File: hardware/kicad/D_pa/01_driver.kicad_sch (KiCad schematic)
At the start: 27 parts, among them J10 A kartindan TX1, Q20 IRF530N, Q21 IRF530N, T10 BN43-202 2:1, T12 BN43-202 2:3 CT, U10 PE4312C-Z, U11 PGA-103+

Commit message: Replace the transmit filters: harmonic suppression was illegal
Simulation of the output filters shows second-harmonic suppression
between 3 and 30 dB, where 43 dB is necessary below 30 MHz and 60 dB
above. On the 80/60 m position the second harmonic of 3.5 MHz is
3.4 dB down: the filter barely touches it. The transmitter would have
been out of specification on every band, and the board gives no sign
of it. Output power, SWR and efficiency all read correctly while the
harmonic radiates.

The cause is the band grouping. One position must pass 5.37 MHz, so
its cutoff is at 6.0, and the second harmonic of the same position's
lowest band, 3.5 MHz, falls at 7.0. More poles do not help: by the
Chebyshev attenuation formula, nine poles give 32 dB there.

Each series inductor now has a parallel capacitor that places a
transmission zero on the harmonic. 80 m and 60 m are separate
positions, because a trap at 7.0 MHz also attenuates a 5.37 MHz
passband. That uses the seventh relay, which was a bypass; a
transmitter with no harmonic filter in line is not legal in any case.

  band      loss   2nd harmonic   was
  160m      0.61   -82.4          -25.2
  80m       0.64   -80.7          grouped
  60m       0.45   -81.9          grouped
  40_30m    1.45   -58.0          -9.5
  20_17m    0.88   -68.4          -18.2
  15_10m    1.35   -61.0          -14.1
  6m        1.14   -82.8          -30.2
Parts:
- removed C110: 10uF, Capacitor_SMD:C_1206_3216Metric, symbol Device:C
- removed C110: 100nF, Capacitor_SMD:C_0603_1608Metric, symbol Device:C
- added C110: 100nF, Capacitor_SMD:C_0603_1608Metric, symbol Device:C
- added C110: 10uF, Capacitor_SMD:C_1206_3216Metric, symbol Device:C
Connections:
- net +3V3: now also C110.1
- net D2_CT: now also C110.1
- net GND: now also C110.2, C110.2

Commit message: Update the ARDC package and record the simulation results
The package had drifted from the boards again: board C's BOM was 45
lines out of date and D's 46, and the schematic PDFs predated both
filter redesigns.

The verification document gains a section on circuit simulation. Every
check before it asks which pin joins which net; none of them can say
whether a capacitor's value is correct. That section holds the
measurements for both redesigns and, separately, the three faults the
simulation tools had themselves: a source divider that made every
insertion loss 6 dB too pessimistic, an E12 rounding helper that
multiplied instead of dividing, and an inductor loss computed at a
fixed 1 MHz.

Two entries in the status were wrong. Gateware timing is closed, with
all five clocks above target rather than two below. Decoupling
placement is corrected. In their place: the remaining overlaps at the
time of writing, five points that still need datasheet confirmation,
and the stock status of the new filter values, which could not be
queried and should be checked before ordering.
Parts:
- removed C110: 100nF, Capacitor_SMD:C_0603_1608Metric, symbol Device:C
- removed C110: 10uF, Capacitor_SMD:C_1206_3216Metric, symbol Device:C
- added C110: 100nF, Capacitor_SMD:C_0603_1608Metric, symbol Device:C
- added C110: 10uF, Capacitor_SMD:C_1206_3216Metric, symbol Device:C
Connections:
- net +3V3: now also C110.1
- net D2_CT: now also C110.1
- net GND: now also C110.2, C110.2

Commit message: Name the copyright holder and stamp it into the generated files
The repository had three licence files and no statement of who owns
the work. The only record of authorship was the git author field.

Copyleft depends on that statement. GPL and CERN-OHL-S work because
the holder grants permission on condition of reciprocity; with no
holder named there is nobody to require it from a downstream user.
Naming the author keeps the design open rather than closing it.

kicad/telif.py is the single source. The line reaches the schematics
through their title block and not through the generators, because
every schematic file is rewritten on each build and a header placed in
a generator would disappear at the first regeneration. All 23
schematics carry it. 109 source files have SPDX headers, split by the
project's own table: generators and the layout chain are hardware
under CERN-OHL-S-2.0, HDL and the audit tools are software under
GPL-3.0-only.

Board C's inductors also move to footprints that match parts that can
be bought. All of them sat on 0805 pads. Of the values this design
needs, 33 to 220 nH are 0603 parts, 470 and 820 nH are 0805, and
everything from 1000 nH upward is 1210, which is 3.2 by 2.5 mm and
does not fit an 0805 land. 32 inductors could not have been soldered.

A symbol-against-footprint check cannot find this. Those two agreed
with each other; what was wrong was the body size of the real part
behind the footprint.
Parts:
- removed C110: 100nF, Capacitor_SMD:C_0603_1608Metric, symbol Device:C
- removed C110: 10uF, Capacitor_SMD:C_1206_3216Metric, symbol Device:C
- added C110: 10uF, Capacitor_SMD:C_1206_3216Metric, symbol Device:C
- added C110: 100nF, Capacitor_SMD:C_0603_1608Metric, symbol Device:C
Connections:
- net +3V3: now also C110.1
- net D2_CT: now also C110.1
- net GND: now also C110.2, C110.2

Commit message: Correct the voltage rating of the RF capacitors on board D
The BOM had no verified order code for 245 parts. The BOM program
recognised the format of a value and wrote "BASE" for all of them. It
did not examine availability.

A new tool queries the supplier. It does not accept "the part
exists". The package and the value must agree exactly. The stock must
be more than the quantity. It also reads the properties of the part.

Two faults came out of this:

The trap capacitors were 50 V parts. The carrier peak voltage is
100 V at 100 W into 50 ohms, and the voltage across the trap inductor
is 93 V. A 50 V part shows the same value in the catalogue and then
breaks down. The fault appears only when the transmitter operates.

The 1.1 pF, 1.6 pF and 3.6 pF values had no stock in the 1206
package. The same values are available in 0603 at 250 V. The smaller
package is acceptable here. This capacitor is the small half of a
pair and carries a small part of the current.

The value selection now depends on availability. The program found
the nearest pair mathematically, and one value was 3.6 pF. That value
has no stock at 250 V in any package. The small half now comes from a
list of parts that are really in stock.

The harmonic suppression did not change: 58.7 dB to 83.8 dB, against
a limit of 43 dB and 60 dB.

The filter capacitors were X7R parts. The capacitance of X7R changes
with voltage and with temperature. Every capacitor below 10 nF is now
a filter part and must be C0G or NP0.

Through-hole parts do not go into machine assembly. A separate file
lists them with the necessary specification. The BOM gave only the
value and a general footprint, and that invites the wrong purchase.
At 100 W, 1.3 A flows through the shunt capacitor at 14 MHz. A cheap
disc ceramic heats, its capacitance moves, and the filter changes.
Only full transmitter power shows this.
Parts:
- removed C110: 10uF, Capacitor_SMD:C_1206_3216Metric, symbol Device:C
- removed C110: 100nF, Capacitor_SMD:C_0603_1608Metric, symbol Device:C
- added C110: 100nF, Capacitor_SMD:C_0603_1608Metric, symbol Device:C
- added C110: 10uF, Capacitor_SMD:C_1206_3216Metric, symbol Device:C
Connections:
- net +3V3: now also C110.1
- net D2_CT: now also C110.1
- net GND: now also C110.2, C110.2

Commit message: Correct the transmit envelope and add a third zero on 15 m to 10 m
The unit has no reconstruction filter. A comment on board A said that
the filter is on board C. Board C has no such filter: the transmit
signal enters through an SMA connector and goes to the transmit and
receive relay. The datasheet also gave a cutoff frequency for this
filter that does not exist.

A sampling DAC does not make one frequency. It makes images at
|k*fs +/- fd|. The zero-order hold gives each image a different
level, and the function falls slowly. If the carrier is near Nyquist,
an image at a lower frequency can be stronger than the carrier.

A new tool measures this. It uses the harmonic filter of board D,
because that filter is the only one in the transmit path.

  15 m to 10 m   4-channel   image at 10.3 MHz is 10.4 dB stronger
  6 m            4-channel   image is 14.2 dB stronger
  6 m            2-channel   image is 7.4 dB stronger
  20 m, 17 m     4-channel   -12.0 dBc, the limit is -43 dBc
  15 m to 10 m   2-channel   -40.4 dBc, the limit is -43 dBc

Only the last one is correctable.

That filter position must attenuate three frequencies: 42 MHz (the
second harmonic of 21 MHz), 63 MHz (the third harmonic) and 50.3 MHz
(the DAC image). A five-pole filter has two traps. No pair of trap
frequencies gives more than 1.9 dB of margin, and 1.9 dB is not a
margin: one E24 rounding already cost 19 dB in this project.

A shunt series-LC at the output adds a third zero. The image goes
from -40.4 dBc to -47.3 dBc, and the margin becomes 23 dB. Above
resonance the branch is capacitive and attenuates the whole stopband,
so the harmonics also improve. The passband loss falls from 1.35 dB
to 0.99 dB.

The transmit envelope is now written honestly. The RTL said "Nyquist
is 20 MHz, so 160 m to 17 m". Nyquist alone is not enough: the images
must also be filtered, and the real limit is lower.

  4-channel   160 m to 30 m
  2-channel   160 m to 10 m
  6 m         no transmit. Receive works, with 68 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
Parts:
- removed C110: 100nF, Capacitor_SMD:C_0603_1608Metric, symbol Device:C
- removed C110: 10uF, Capacitor_SMD:C_1206_3216Metric, symbol Device:C
- added C110: 100nF, Capacitor_SMD:C_0603_1608Metric, symbol Device:C
- added C110: 10uF, Capacitor_SMD:C_1206_3216Metric, symbol Device:C
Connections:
- net +3V3: now also C110.1
- net D2_CT: now also C110.1
- net GND: now also C110.2, C110.2

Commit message: Add BIAS_KILL to remove a single-fault destruction path
Each final device has its own closed-loop bias servo: a 0.01 ohm
sense resistor, an INA240A1 with a gain of 20, an LM358 integrator,
and the gate. Separate servos are correct for paralleled MOSFETs,
because different threshold voltages make one device take most of the
current.

A new tool measures the loop in ngspice. It does not model the inside
of the MOSFET. The boundary conditions are sufficient: input
capacitance, transconductance and threshold voltage.

The loop is stable. The crossover is at 25.7 Hz, the phase margin is
90 degrees, and the current reaches the set value in 106 ms.

The failure behaviour is destructive. The integrator raises the gate
until the measured current equals the set value. If the measurement
arm opens, the measured current reads zero. The error never closes.

  the gate reaches 10.4 V in 285 ms
  57.6 A and 2878 W in each device
  the continuous limit of the IRFP250N is 214 W

All four devices fail. The protection circuit kills what it protects.

A zener clamp does not solve this. The transconductance is 8 S, so
1 V above the threshold already gives 8 A. A safe clamp voltage would
be too near the operating point.

The board sees the condition already. Board 06 says: if the quiescent
current differs from the set value by 20 percent, the bias servo is
faulty, so cut. But PA_INHIBIT removes only the driver supply. In a
class-A stage the quiescent current does the damage, not the drive.

BIAS_KILL short-circuits the integrator capacitor. A pull-down on the
gate alone is not sufficient: the integrator would stay charged at
the rail, and the gate would jump to 10.5 V when the fault clears.
With the capacitor short-circuited, the op-amp follows the set
voltage and the gate stays at 0.33 V. The threshold is 3.2 V.

The circuit is one 2N7002 that inverts PA_INHIBIT, a 10k pull-up, and
one 2N7002 across each integrator capacitor. The unpowered state is
safe: the 10k pull-downs hold the gate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
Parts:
- removed C110: 100nF, Capacitor_SMD:C_0603_1608Metric, symbol Device:C
- removed C110: 10uF, Capacitor_SMD:C_1206_3216Metric, symbol Device:C
- added C110: 10uF, Capacitor_SMD:C_1206_3216Metric, symbol Device:C
- added C110: 100nF, Capacitor_SMD:C_0603_1608Metric, symbol Device:C
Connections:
- net +3V3: now also C110.1
- net D2_CT: now also C110.1
- net GND: now also C110.2, C110.2

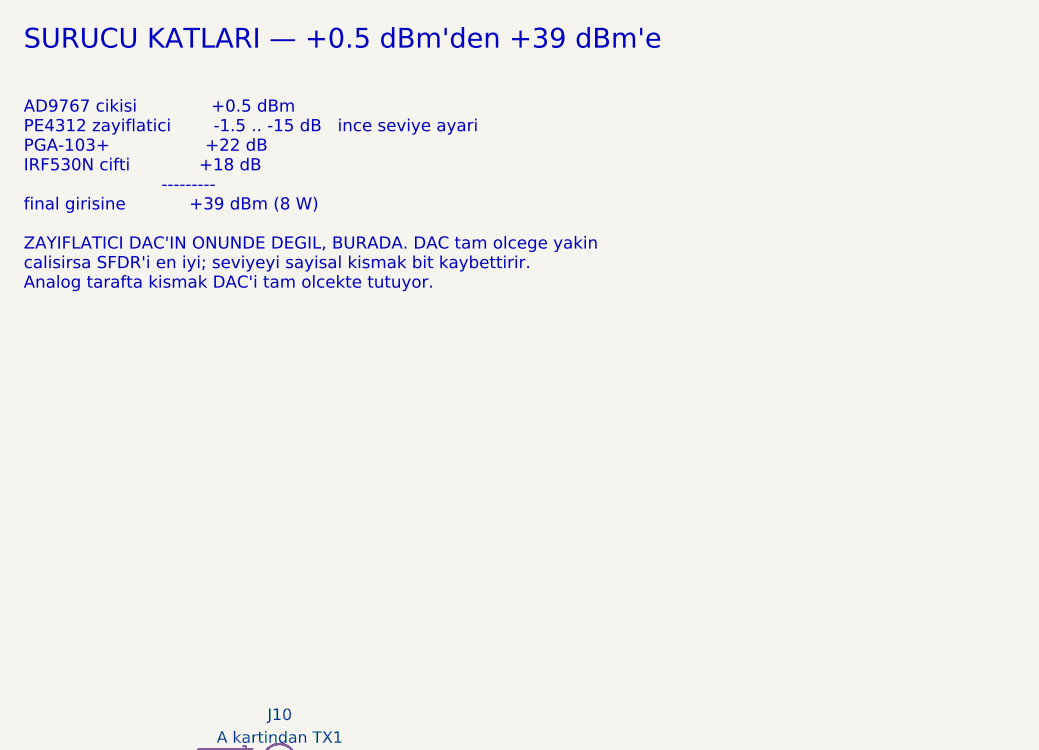
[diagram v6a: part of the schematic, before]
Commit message: Give the drive level that the final stage really needs
The budget on the schematic added the driver stages. It did not say
how much drive the final stage needs. Without that number, nobody can
tell whether the budget closes.

A new tool calculates both sides from the devices.

The output side is healthy. The quiescent current is 6.68 A, and in
class A the peak current cannot go above it. 100 W needs a peak
voltage of 29.9 V against a 50 V supply. The margin is 40 percent,
so there is no saturation risk.

The drive side is small. The gate node of each arm has a 1 ohm
swamping resistor. The value is not arbitrary: the reactance of the
input capacitance is 1.02 ohms at 30 MHz, so a resistor of the same
order makes the input independent of frequency. The gate swing is
3.34 A peak divided by 8 S, which is 0.42 V peak. The real power is
87 mW in each arm. Two arms give 174 mW, which is +22.4 dBm.

The chain can give +39.0 dBm. The difference is 16.6 dB. This is not
a defect. It is the range of the attenuator.

But the schematic said "+39 dBm (8 W) to the final input", and that
reads as if the final stage takes 8 W of drive. It does not.

The condition is now written next to the budget: the attenuator must
start at maximum attenuation. A 0 dB default overdrives the stage by
17 dB. The stage then clips, and the harmonic filter receives a stage
that makes exactly what the filter must remove.
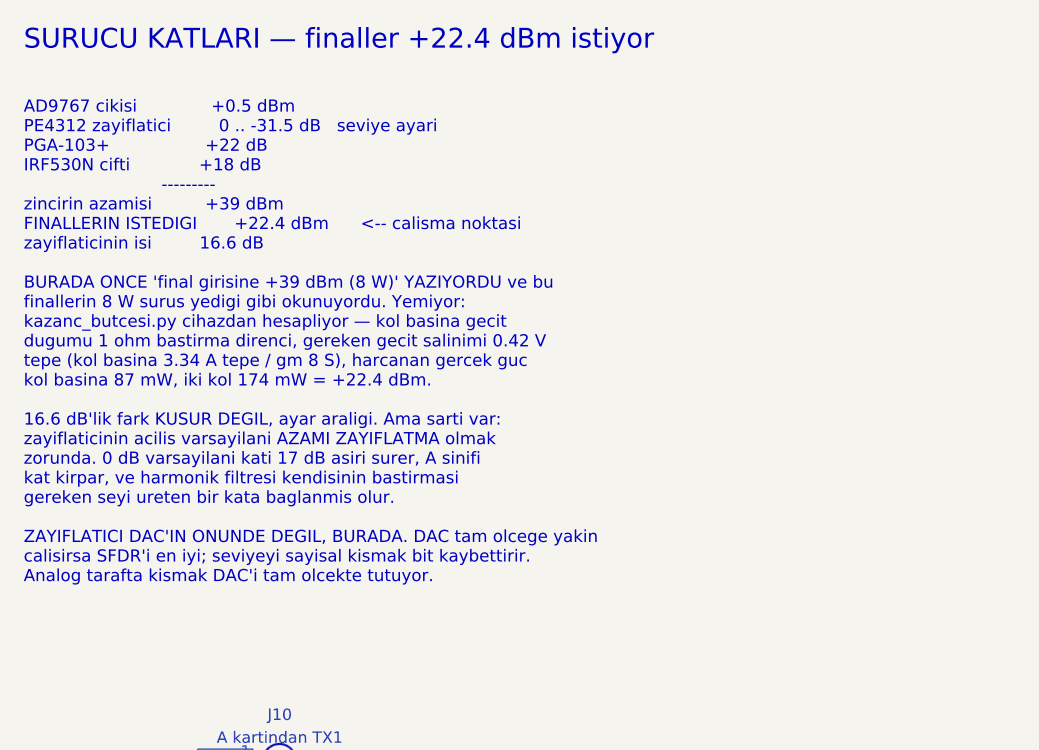
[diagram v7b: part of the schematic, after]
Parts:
- removed C110: 10uF, Capacitor_SMD:C_1206_3216Metric, symbol Device:C
- removed C110: 100nF, Capacitor_SMD:C_0603_1608Metric, symbol Device:C
- added C110: 100nF, Capacitor_SMD:C_0603_1608Metric, symbol Device:C
- added C110: 10uF, Capacitor_SMD:C_1206_3216Metric, symbol Device:C
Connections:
- net +3V3: now also C110.1
- net D2_CT: now also C110.1
- net GND: now also C110.2, C110.2
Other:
- note added: "AD9767 cikisi +0.5 dBm PE4312 zayiflatici 0 .. -31.5 dB seviye ayari PGA-103+ +22 dB IRF530N cifti +18 dB --------- zincirin azamisi +39 dBm FINALLERIN ISTEDIGI +22.4 dBm <-- calisma noktasi zayiflaticinin isi 16.6 dB BURADA ONCE 'final girisine +39 dBm (8 W)' YAZIYORDU ve bu finallerin 8 W surus yedigi gibi okunuyordu. Yemiyor: kazanc_butcesi.py cihazdan hesapliyor — kol basina gecit dugumu 1 oh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"
- note added: "SURUCU KATLARI — finaller +22.4 dBm istiyor"
- note removed: "AD9767 cikisi +0.5 dBm PE4312 zayiflatici -1.5 .. -15 dB ince seviye ayari PGA-103+ +22 dB IRF530N cifti +18 dB --------- final girisine +39 dBm (8 W) ZAYIFLATICI DAC'IN ONUNDE DEGIL, BURADA. DAC tam olcege yakin calisirsa SFDR'i en iyi; seviyeyi sayisal kismak bit kaybettirir. Analog tarafta kismak DAC'i tam olcekte tutuyor."
- note removed: "SURUCU KATLARI — +0.5 dBm'den +39 dBm'e"
